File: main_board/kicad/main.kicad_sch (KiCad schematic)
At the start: 36 parts, among them J1 Sensorbuchse, J2 Motorbuchse, J3 Motorbuchse, J4 Batteriebuchse, J5 Conn_02x07_Odd_Even, J6 Sensorbuchse, J7 AVR-ISP-10, U100 Board_LST, U6 74HC14

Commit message: added footprints
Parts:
- C32: footprint (none) -> Capacitor_THT:C_Disc_D3.0mm_W1.6mm_P2.50mm
- D21, D22, D23, D24, D25, D26, D27, D28, D29, D30: footprint (none) -> LED_THT:LED_D5.0mm
- J5: footprint (none) -> Connector_IDC:IDC-Header_2x07_P2.54mm_Horizontal
- R20, R21, R22, R23, R24, R25, R44, R45, R46, R47, R48, R49, R50, R51, R52, R53: footprint (none) -> Resistor_THT:R_Axial_DIN0207_L6.3mm_D2.5mm_P7.62mm_Horizontal
- U6: footprint (none) -> Package_DIP:DIP-14_W10.16mm_LongPads
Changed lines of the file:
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@@
       (effects (font (size 1.27 1.27)))
     )
-    (property "Footprint" "" (at 99.06 137.16 0)
+    (property "Footprint" "LED_THT:LED_D5.0mm" (at 99.06 137.16 0)
       (effects (font (size 1.27 1.27)) hide)
     )
@@
       (effects (font (size 1.27 1.27)))
     )
-    (property "Footprint" "" (at 118.11 137.16 0)
+    (property "Footprint" "Package_DIP:DIP-14_W10.16mm_LongPads" (at 118.11 137.16 0)
       (effects (font (size 1.27 1.27)) hide)
     )
@@
       (effects (font (size 1.27 1.27)))
     )
-    (property "Footprint" "" (at 99.06 41.91 0)
+    (property "Footprint" "LED_THT:LED_D5.0mm" (at 99.06 41.91 0)
       (effects (font (size 1.27 1.27)) hide)
     )
@@
       (effects (font (size 1.27 1.27)))
     )
-    (property "Footprint" "" (at 109.22 85.598 90)
+    (property "Footprint" "Resistor_THT:R_Axial_DIN0207_L6.3mm_D2.5mm_P7.62mm_Horizontal" (at 109.22 85.598 90)
       (effects (font (size 1.27 1.27)) hide)
     )
@@
       (effects (font (size 1.27 1.27)))
     )
-    (property "Footprint" "" (at 106.68 166.878 90)
+    (property "Footprint" "Resistor_THT:R_Axial_DIN0207_L6.3mm_D2.5mm_P7.62mm_Horizontal" (at 106.68 166.878 90)
       (effects (font (size 1.27 1.27)) hide)
     )
@@
       (effects (font (size 1.27 1.27)))
     )
-    (property "Footprint" "" (at 97.79 182.372 90)
+    (property "Footprint" "Resistor_THT:R_Axial_DIN0207_L6.3mm_D2.5mm_P7.62mm_Horizontal" (at 97.79 182.372 90)
       (effects (font (size 1.27 1.27)) hide)
     )
@@
       (effects (font (size 1.27 1.27)))
     )
-    (property "Footprint" "" (at 106.68 71.628 90)
+    (property "Footprint" "Resistor_THT:R_Axial_DIN0207_L6.3mm_D2.5mm_P7.62mm_Horizontal" (at 106.68 71.628 90)
       (effects (font (size 1.27 1.27)) hide)
     )
@@
       (effects (font (size 1.27 1.27)))
     )
-    (property "Footprint" "" (at 116.84 177.292 90)
+    (property "Footprint" "Resistor_THT:R_Axial_DIN0207_L6.3mm_D2.5mm_P7.62mm_Horizontal" (at 116.84 177.292 90)
       (effects (font (size 1.27 1.27)) hide)
     )
@@
       (effects (font (size 1.27 1.27)) (justify right))
     )
-    (property "Footprint" "" (at 104.902 99.06 90)
+    (property "Footprint" "Resistor_THT:R_Axial_DIN0207_L6.3mm_D2.5mm_P7.62mm_Horizontal" (at 104.902 99.06 90)
       (effects (font (size 1.27 1.27)) hide)
     )
@@
       (effects (font (size 1.27 1.27)))
     )
-    (property "Footprint" "" (at 118.11 165.1 0)
+    (property "Footprint" "Package_DIP:DIP-14_W10.16mm_LongPads" (at 118.11 165.1 0)
       (effects (font (size 1.27 1.27)) hide)
     )
@@
       (effects (font (size 1.27 1.27)) (justify left))
     )
-    (property "Footprint" "" (at 44.45 151.13 0)
+    (property "Footprint" "Package_DIP:DIP-14_W10.16mm_LongPads" (at 44.45 151.13 0)
       (effects (font (size 1.27 1.27)) hide)
     )
@@
       (effects (font (size 1.27 1.27)))
     )
-    (property "Footprint" "" (at 106.68 138.938 90)
+    (property "Footprint" "Resistor_THT:R_Axial_DIN0207_L6.3mm_D2.5mm_P7.62mm_Horizontal" (at 106.68 138.938 90)
       (effects (font (size 1.27 1.27)) hide)
     )
@@
       (effects (font (size 1.27 1.27)))
     )
-    (property "Footprint" "" (at 106.68 43.688 90)
+    (property "Footprint" "Resistor_THT:R_Axial_DIN0207_L6.3mm_D2.5mm_P7.62mm_Horizontal" (at 106.68 43.688 90)
       (effects (font (size 1.27 1.27)) hide)
     )
@@
       (effects (font (size 1.27 1.27)))
     )
-    (property "Footprint" "" (at 99.06 165.1 0)
+    (property "Footprint" "LED_THT:LED_D5.0mm" (at 99.06 165.1 0)
       (effects (font (size 1.27 1.27)) hide)
     )
@@
       (effects (font (size 1.27 1.27)))
     )
-    (property "Footprint" "" (at 107.95 179.832 90)
+    (property "Footprint" "Resistor_THT:R_Axial_DIN0207_L6.3mm_D2.5mm_P7.62mm_Horizontal" (at 107.95 179.832 90)
       (effects (font (size 1.27 1.27)) hide)
     )
@@
       (effects (font (size 1.27 1.27)))
     )
-    (property "Footprint" "" (at 118.11 55.88 0)
+    (property "Footprint" "Package_DIP:DIP-14_W10.16mm_LongPads" (at 118.11 55.88 0)
       (effects (font (size 1.27 1.27)) hide)
     )
@@
       (effects (font (size 1.27 1.27)))
     )
-    (property "Footprint" "" (at 116.84 23.622 90)
+    (property "Footprint" "Resistor_THT:R_Axial_DIN0207_L6.3mm_D2.5mm_P7.62mm_Horizontal" (at 116.84 23.622 90)
       (effects (font (size 1.27 1.27)) hide)
     )
@@
       (effects (font (size 1.27 1.27)))
     )
-    (property "Footprint" "" (at 125.73 21.082 90)
+    (property "Footprint" "Resistor_THT:R_Axial_DIN0207_L6.3mm_D2.5mm_P7.62mm_Horizontal" (at 125.73 21.082 90)
       (effects (font (size 1.27 1.27)) hide)
     )
@@
       (effects (font (size 1.27 1.27)))
     )
-    (property "Footprint" "" (at 133.096 104.14 0)
+    (property "Footprint" "LED_THT:LED_D5.0mm" (at 133.096 104.14 0)
       (effects (font (size 1.27 1.27)) hide)
     )
@@
       (effects (font (size 1.27 1.27)))
     )
-    (property "Footprint" "" (at 99.06 151.13 0)
+    (property "Footprint" "LED_THT:LED_D5.0mm" (at 99.06 151.13 0)
       (effects (font (size 1.27 1.27)) hide)
     )
@@
       (effects (font (size 1.27 1.27)))
     )
-    (property "Footprint" "" (at 110.744 104.14 0)
+    (property "Footprint" "LED_THT:LED_D5.0mm" (at 110.744 104.14 0)
       (effects (font (size 1.27 1.27)) hide)
     )
@@
       (effects (font (size 1.27 1.27)) (justify right))
     )
-    (property "Footprint" "" (at 135.382 109.22 90)
+    (property "Footprint" "Resistor_THT:R_Axial_DIN0207_L6.3mm_D2.5mm_P7.62mm_Horizontal" (at 135.382 109.22 90)
       (effects (font (size 1.27 1.27)) hide)
     )
@@
       (effects (font (size 1.27 1.27)) (justify right))
     )
-    (property "Footprint" "" (at 86.36 101.6 0)
+    (property "Footprint" "Connector_IDC:IDC-Header_2x07_P2.54mm_Horizontal" (at 86.36 101.6 0)
       (effects (font (size 1.27 1.27)) hide)
     )
@@
       (effects (font (size 1.27 1.27)))
     )
-    (property "Footprint" "" (at 107.95 26.162 90)
+    (property "Footprint" "Resistor_THT:R_Axial_DIN0207_L6.3mm_D2.5mm_P7.62mm_Horizontal" (at 107.95 26.162 90)
       (effects (font (size 1.27 1.27)) hide)
     )
@@
       (effects (font (size 1.27 1.27)))
     )
-    (property "Footprint" "" (at 118.11 69.85 0)
+    (property "Footprint" "Package_DIP:DIP-14_W10.16mm_LongPads" (at 118.11 69.85 0)
       (effects (font (size 1.27 1.27)) hide)
     )
@@
       (effects (font (size 1.27 1.27)))
     )
-    (property "Footprint" "" (at 99.06 55.88 0)
+    (property "Footprint" "LED_THT:LED_D5.0mm" (at 99.06 55.88 0)
       (effects (font (size 1.27 1.27)) hide)
     )
@@
       (effects (font (size 1.27 1.27)) (justify left))
     )
-    (property "Footprint" "" (at 99.06 119.38 0)
+    (property "Footprint" "LED_THT:LED_D5.0mm" (at 99.06 119.38 0)
       (effects (font (size 1.27 1.27)) hide)
     )
@@
       (effects (font (size 1.27 1.27)))
     )
-    (property "Footprint" "" (at 99.06 69.85 0)
+    (property "Footprint" "LED_THT:LED_D5.0mm" (at 99.06 69.85 0)
       (effects (font (size 1.27 1.27)) hide)
     )
@@
       (effects (font (size 1.27 1.27)) (justify right))
     )
-    (property "Footprint" "" (at 99.06 87.63 0)
+    (property "Footprint" "LED_THT:LED_D5.0mm" (at 99.06 87.63 0)
       (effects (font (size 1.27 1.27)) hide)
     )
@@
       (effects (font (size 1.27 1.27)))
     )
-    (property "Footprint" "" (at 109.22 124.968 90)
+    (property "Footprint" "Resistor_THT:R_Axial_DIN0207_L6.3mm_D2.5mm_P7.62mm_Horizontal" (at 109.22 124.968 90)
       (effects (font (size 1.27 1.27)) hide)
     )
@@
       (effects (font (size 1.27 1.27)))
     )
-    (property "Footprint" "" (at 118.11 151.13 0)
+    (property "Footprint" "Package_DIP:DIP-14_W10.16mm_LongPads" (at 118.11 151.13 0)
       (effects (font (size 1.27 1.27)) hide)
     )
@@
       (effects (font (size 1.27 1.27)) (justify left))
     )
-    (property "Footprint" "" (at 30.1752 153.67 0)
+    (property "Footprint" "Capacitor_THT:C_Disc_D3.0mm_W1.6mm_P2.50mm" (at 30.1752 153.67 0)
       (effects (font (size 1.27 1.27)) hide)
     )
@@
       (effects (font (size 1.27 1.27)))
     )
-    (property "Footprint" "" (at 106.68 152.908 90)
+    (property "Footprint" "Resistor_THT:R_Axial_DIN0207_L6.3mm_D2.5mm_P7.62mm_Horizontal" (at 106.68 152.908 90)
       (effects (font (size 1.27 1.27)) hide)
     )
@@
       (effects (font (size 1.27 1.27)))
     )
-    (property "Footprint" "" (at 118.11 41.91 0)
+    (property "Footprint" "Package_DIP:DIP-14_W10.16mm_LongPads" (at 118.11 41.91 0)
       (effects (font (size 1.27 1.27)) hide)
     )
@@
       (effects (font (size 1.27 1.27)))
     )
-    (property "Footprint" "" (at 106.68 57.658 90)
-      (effects (font (size 1.27 1.27)) hide)
-    )
+    (property "Footprint" "Resistor_THT:R_Axial_DIN0207_L6.3mm_D2.5mm_P7.62mm_Horizontal" (at 106.68 57.658 90)
+      (effects (font (size 1.27 1.27)) hide)
+    )

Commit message: implemented bridge and first bridge driver as well as both step converters on the pcd layout
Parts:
- J7: footprint Connector_IDC:IDC-Header_2x05_P2.54mm_Vertical -> Connector_IDC:IDC-Header_2x06_P2.54mm_Horizontal
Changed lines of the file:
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@@
       (effects (font (size 1.27 1.27)) (justify right))
     )
-    (property "Footprint" "Connector_IDC:IDC-Header_2x05_P2.54mm_Vertical" (at 39.37 72.39 90)
+    (property "Footprint" "Connector_IDC:IDC-Header_2x06_P2.54mm_Horizontal" (at 39.37 72.39 90)
       (effects (font (size 1.27 1.27)) hide)
     )

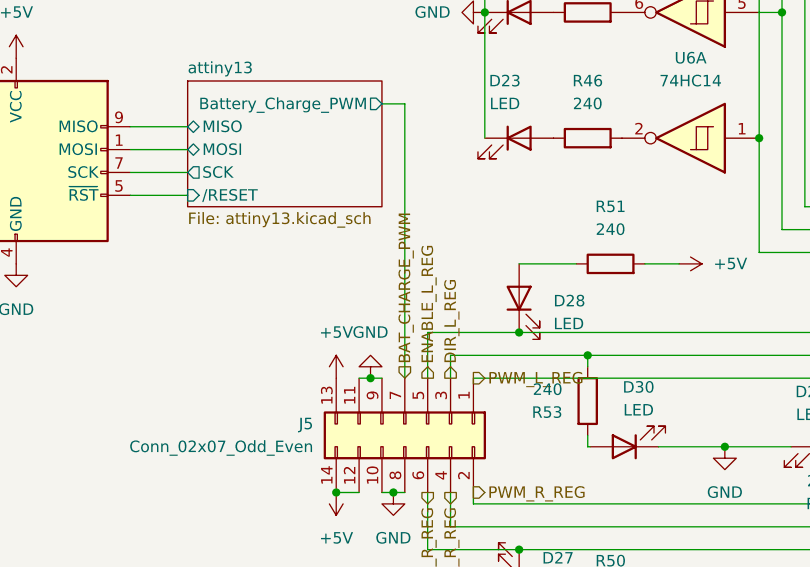
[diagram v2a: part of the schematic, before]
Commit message: rerouted more lines, also implemented HAL LEDS
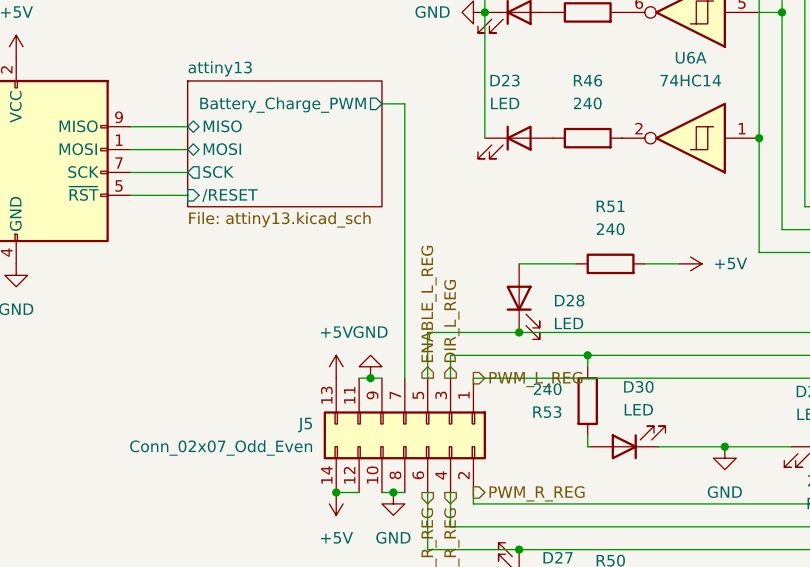
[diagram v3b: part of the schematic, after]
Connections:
- net BAT_CHARGE_PWM renamed attiny13/Battery_Charge_PWM
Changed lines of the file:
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@@
+    (stroke (width 0) (type default))
+  )
+  (wire (pts (xy 55.88 68.58) (xy 62.23 68.58))
     (stroke (width 0) (type default))
   )
@@
   )
   (wire (pts (xy 125.73 137.16) (xy 130.81 137.16))
-    (stroke (width 0) (type default))
-  )
-  (wire (pts (xy 55.88 68.58) (xy 62.23 68.58))
     (stroke (width 0) (type default))
   )
@@
   )
   (hierarchical_label "DIR_L_REG" (shape output) (at 91.44 96.52 90) (fields_autoplaced)
-    (effects (font (size 1.27 1.27)) (justify left))
-  )
-  (hierarchical_label "BAT_CHARGE_PWM" (shape input) (at 86.36 96.52 90) (fields_autoplaced)
     (effects (font (size 1.27 1.27)) (justify left))
   )
@@
   )
   (symbol (lib_id "Connector_Generic:Conn_02x07_Odd_Even") (at 86.36 101.6 270) (unit 1)
-    (in_bom yes) (on_board yes) (dnp no) (fields_autoplaced)
+    (in_bom yes) (on_board yes) (dnp no)
     (property "Reference" "J5" (at 76.2 101.6 90)
       (effects (font (size 1.27 1.27)) (justify right))
